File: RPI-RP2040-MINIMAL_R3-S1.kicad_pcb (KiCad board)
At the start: 2 copper layers, 65 x 67 mm, 31 parts, among them J3 Conn_01x04_Pin, J4 Conn_01x04_Socket, P1 USB_C_Plug_USB2.0, U1 NCP1117ST33T3G, U2 W25Q128JVSIQ, U3 RP2040, X1 12MHz

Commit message: flip connector in schematic but not pcb i cant update pcb pls help
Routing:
- added copper zone on F.Cu, net (none)
- removed copper zone on F.Cu, net +1V1
- removed copper zone on F.Cu, net +3V3

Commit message: swap connectors, fix button position
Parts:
- moved J3 13.7 mm to (96.3, 75.1)
- moved J4 13.5 mm to (103.9, 60.3)
- moved ESTOP1 9.90 mm to (54.3, 91.3)
- moved P1 3.50 mm to (100.0, 40.1)
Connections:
- J3 pad 1: Net-(J3-Pin_1) -> GND
- J3 pad 2: unconnected-(J3-Pin_2-Pad2) -> /USB_D+
- J3 pad 3: Net-(J3-Pin_3) -> /USB_D-
- J3 pad 4: Net-(J3-Pin_4) -> VBUS
- J4 pad 1: GND -> /BRIDGE_GND
- J4 pad 2: /USB_D+ -> /BRIDGE_USBD+
- J4 pad 3: /USB_D- -> /BRIDGE_USBD-
- J4 pad 4: VBUS -> /BRIDGE_VBUS
- P1 pad A1: Net-(J3-Pin_1) -> /BRIDGE_GND
- P1 pad A12: Net-(J3-Pin_1) -> /BRIDGE_GND
- P1 pad A4: Net-(J3-Pin_4) -> /BRIDGE_VBUS
- P1 pad A5: Net-(J3-Pin_4) -> /BRIDGE_VBUS
- P1 pad A6: unconnected-(J3-Pin_2-Pad2) -> /BRIDGE_USBD+
- P1 pad A7: Net-(J3-Pin_3) -> /BRIDGE_USBD-
- P1 pad A9: Net-(J3-Pin_4) -> /BRIDGE_VBUS
- P1 pad B1: Net-(J3-Pin_1) -> /BRIDGE_GND
- P1 pad B12: Net-(J3-Pin_1) -> /BRIDGE_GND
- P1 pad B4: Net-(J3-Pin_4) -> /BRIDGE_VBUS
- P1 pad B9: Net-(J3-Pin_4) -> /BRIDGE_VBUS
- P1 pad SH: Net-(J3-Pin_1) -> /BRIDGE_GND
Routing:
- net /BRIDGE_USBD-: track 0.00 -> 22.1 mm
- net /BRIDGE_USBD+: track 0.00 -> 19.8 mm, vias 0 -> 2
- net Net-(J3-Pin_3): track 16.9 -> 0.00 mm
- net unconnected-(J3-Pin_2-Pad2): track 16.9 -> 0.00 mm
- net /USB_D-: track 33.0 -> 19.1 mm
- net VBUS: track 19.8 -> 7.29 mm
- net /BRIDGE_GND: track 0.00 -> 12.1 mm, vias 0 -> 2
- net +3V3: track 28.8 -> 19.2 mm
- net /GPIO0: track 36.2 -> 40.3 mm
- net /USB_D+: track 21.0 -> 19.1 mm
- net Net-(J3-Pin_1): vias 2 -> 0
- added copper zone on F.Cu, net +3V3
- added copper zone on B.Cu, net /BRIDGE_GND
- added copper zone on F.Cu, net /BRIDGE_VBUS
- removed copper zone on B.Cu, net Net-(J3-Pin_1)
- removed copper zone on F.Cu, net Net-(J3-Pin_1)
- removed copper zone on F.Cu, net Net-(J3-Pin_4)
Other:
- board size 65 x 67 mm -> 65 x 70.5 mm
- board text added: "5V"
- board text added: "GND"
- board text removed: "GP7"

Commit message: fix 1V1 connection
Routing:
- net +3V3: track 19.2 -> 48.0 mm
- net +1V1: track 14.2 -> 16.2 mm
- added copper zone on F.Cu, net +1V1
- removed copper zone on F.Cu, net (none)
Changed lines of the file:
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@@
 			(disableapertmacros no)
 			(usegerberextensions no)
-			(usegerberattributes no)
+			(usegerberattributes yes)
 			(usegerberadvancedattributes no)
 			(creategerberjobfile no)
@@
 		(tags "tactile switch SPST angled PTS645VL31-2 LFS C&K Button")
 		(property "Reference" "ESTOP1"
-			(at 2.25 1.68 0)
+			(at 2.3025 -3.82 0)
 			(layer "F.SilkS")
 			(effects
@@
 		)
 		(fp_text user "${REFERENCE}"
-			(at 2.25 1.68 0)
+			(at 2.25 -3.82 0)
 			(layer "F.Fab")
 			(effects
@@
 	)
 	(segment
+		(start 99.63 97.745)
+		(end 99.865 97.51)
+		(width 0.15)
+		(layer "F.Cu")
+		(net "+3V3")
+	)
+	(segment
 		(start 103.1025 101.345)
 		(end 105.465 101.345)
@@
 	)
 	(segment
+		(start 99.735 103)
+		(end 97.5 103)
+		(width 0.2)
+		(layer "F.Cu")
+		(net "+3V3")
+	)
+	(segment
+		(start 96.83 101.345)
+		(end 96.89 101.285)
+		(width 0.15)
+		(layer "F.Cu")
+		(net "+3V3")
+	)
+	(segment
+		(start 102.5 101.345)
+		(end 103.065 101.345)
+		(width 0.15)
+		(layer "F.Cu")
+		(net "+3V3")
+	)
+	(segment
+		(start 99.925 103.12)
+		(end 99.865 103.18)
+		(width 0.15)
+		(layer "F.Cu")
+		(net "+3V3")
+	)
+	(segment
 		(start 99.963474 105.954)
 		(end 101.19 105.954)
@@
 	)
 	(segment
+		(start 102.265 101.11)
+		(end 102.5 101.345)
+		(width 0.15)
+		(layer "F.Cu")
+		(net "+3V3")
+	)
+	(segment
+		(start 101.865 96.945)
+		(end 101.865 100.71)
+		(width 0.15)
+		(layer "F.Cu")
+		(net "+3V3")
+	)
+	(segment
+		(start 97 102.5)
+		(end 97 102)
+		(width 0.2)
+		(layer "F.Cu")
+		(net "+3V3")
+	)
+	(segment
 		(start 100.015001 94.457535)
 		(end 100.015001 95.894999)
@@
 	)
 	(segment
+		(start 101.865 100.71)
+		(end 102.5 101.345)
+		(width 0.15)
+		(layer "F.Cu")
+		(net "+3V3")
+	)
+	(segment
 		(start 93.865 101.345)
 		(end 93.665 101.545)
@@
 	)
 	(segment
+		(start 96.83 97.745)
+		(end 96.265 97.745)
+		(width 0.15)
+		(layer "F.Cu")
+		(net "+3V3")
+	)
+	(segment
 		(start 107.665 86.345)
 		(end 107.665 89.345)
@@
 	)
 	(segment
+		(start 100.265 96.945)
+		(end 99.865 96.945)
+		(width 0.15)
+		(layer "F.Cu")
+		(net "+3V3")
+	)
+	(segment
+		(start 99.865 103.745)
+		(end 99.865 103.13)
+		(width 0.2)
+		(layer "F.Cu")
+		(net "+3V3")
+	)
+	(segment
 		(start 96.2275 101.345)
 		(end 93.865 101.345)
@@
 	)
 	(segment
+		(start 97 101.515)
+		(end 96.83 101.345)
+		(width 0.2)
+		(layer "F.Cu")
+		(net "+3V3")
+	)
+	(segment
+		(start 100.725 103.12)
+		(end 99.925 103.12)
+		(width 0.15)
+		(layer "F.Cu")
+		(net "+3V3")
+	)
+	(segment
+		(start 102.5 101.345)
+		(end 100.725 103.12)
+		(width 0.15)
+		(layer "F.Cu")
+		(net "+3V3")
+	)
+	(segment
 		(start 96.315 85.715)
 		(end 96.315 83.195)
@@
 	)
 	(segment
+		(start 99.865 103.18)
+		(end 99.865 103.745)
+		(width 0.15)
+		(layer "F.Cu")
+		(net "+3V3")
+	)
+	(segment
 		(start 99.665 94.107534)
 		(end 100.015001 94.457535)
@@
 	)
 	(segment
+		(start 97 102)
+		(end 97 101.515)
+		(width 0.2)
+		(layer "F.Cu")
+		(net "+3V3")
+	)
+	(segment
+		(start 100.265 97.11)
+		(end 99.865 97.51)
+		(width 0.15)
+		(layer "F.Cu")
+		(net "+3V3")
+	)
+	(segment
+		(start 99.865 97.51)
+		(end 99.865 96.945)
+		(width 0.15)
+		(layer "F.Cu")
+		(net "+3V3")
+	)
+	(segment
 		(start 100.265 96.9075)
 		(end 100.265 96.144998)
@@
 	)
 	(segment
+		(start 102.265 96.945)
+		(end 102.265 101.11)
+		(width 0.15)
+		(layer "F.Cu")
+		(net "+3V3")
+	)
+	(segment
 		(start 99.865 103.745)
 		(end 99.865 105.855526)
@@
 	)
 	(segment
+		(start 96.265 97.745)
+		(end 99.63 97.745)
+		(width 0.15)
+		(layer "F.Cu")
+		(net "+3V3")
+	)
+	(segment
 		(start 99.865 96.045)
 		(end 99.865 96.9075)
@@
 	)
 	(segment
+		(start 96.89 101.285)
+		(end 96.89 97.805)
+		(width 0.15)
+		(layer "F.Cu")
+		(net "+3V3")
+	)
+	(segment
+		(start 99.865 103.13)
+		(end 99.735 103)
+		(width 0.2)
+		(layer "F.Cu")
+		(net "+3V3")
+	)
+	(segment
 		(start 99.665 93.345)
 		(end 99.665 94.107534)
@@
 	)
 	(segment
+		(start 97.5 103)
+		(end 97 102.5)
+		(width 0.2)
+		(layer "F.Cu")
+		(net "+3V3")
+	)
+	(segment
+		(start 96.89 97.805)
+		(end 96.83 97.745)
+		(width 0.15)
+		(layer "F.Cu")
+		(net "+3V3")
+	)
+	(segment
+		(start 100.265 96.945)
+		(end 100.265 97.11)
+		(width 0.15)
+		(layer "F.Cu")
+		(net "+3V3")
+	)
+	(segment
 		(start 99.865 105.855526)
 		(end 99.963474 105.954)
@@
 	)
 	(segment
+		(start 96.83 101.345)
+		(end 96.265 101.345)
+		(width 0.2)
+		(layer "F.Cu")
+		(net "+3V3")
+	)
+	(segment
 		(start 102.971984 105.954)
 		(end 102.97199 105.954006)
@@
 	)
 	(segment
+		(start 100.755 98.245)
+		(end 100.365 98.245)
+		(width 0.15)
+		(layer "F.Cu")
+		(net "+1V1")
+	)
+	(segment
 		(start 100.265 104.424274)
 		(end 100.265 103.745)
@@
 	)
 	(segment
+		(start 101.465 96.945)
+		(end 101.465 97.535)
+		(width 0.15)
+		(layer "F.Cu")
+		(net "+1V1")
+	)
+	(segment
 		(start 100.99 105.045)
 		(end 101.2 104.835)
@@
 	)
 	(segment
+		(start 101.465 97.535)
+		(end 100.755 98.245)
+		(width 0.15)
+		(layer "F.Cu")
+		(net "+1V1")
+	)
+	(segment
 		(start 98.665 93.345)
 		(end 98.665 93.64)
@@
 	)
 	(zone
+		(net "+1V1")
 		(layer "F.Cu")
 		(hatch edge 0.508)
-		(priority 3)
+		(priority 6)
 		(connect_pads yes
 			(clearance 0.15)
@@
 			)
 		)
-	)
-	(zone
-		(layer "F.Cu")
-		(hatch edge 0.508)
-		(priority 1)
-		(connect_pads yes
-			(clearance 0.15)
-		)
-		(min_thickness 0.15)
-		(fill yes
-			(thermal_gap 0.508)
-			(thermal_bridge_width 0.508)
-			(island_removal_mode 0)
-		)
-		(polygon
-			(pts
-				(xy 102.465 103.145) (xy 96.865 103.145) (xy 96.865 97.545) (xy 99.665 97.545) (xy 100.465 97.545)
-				(xy 102.465 97.545)
-			)
-		)

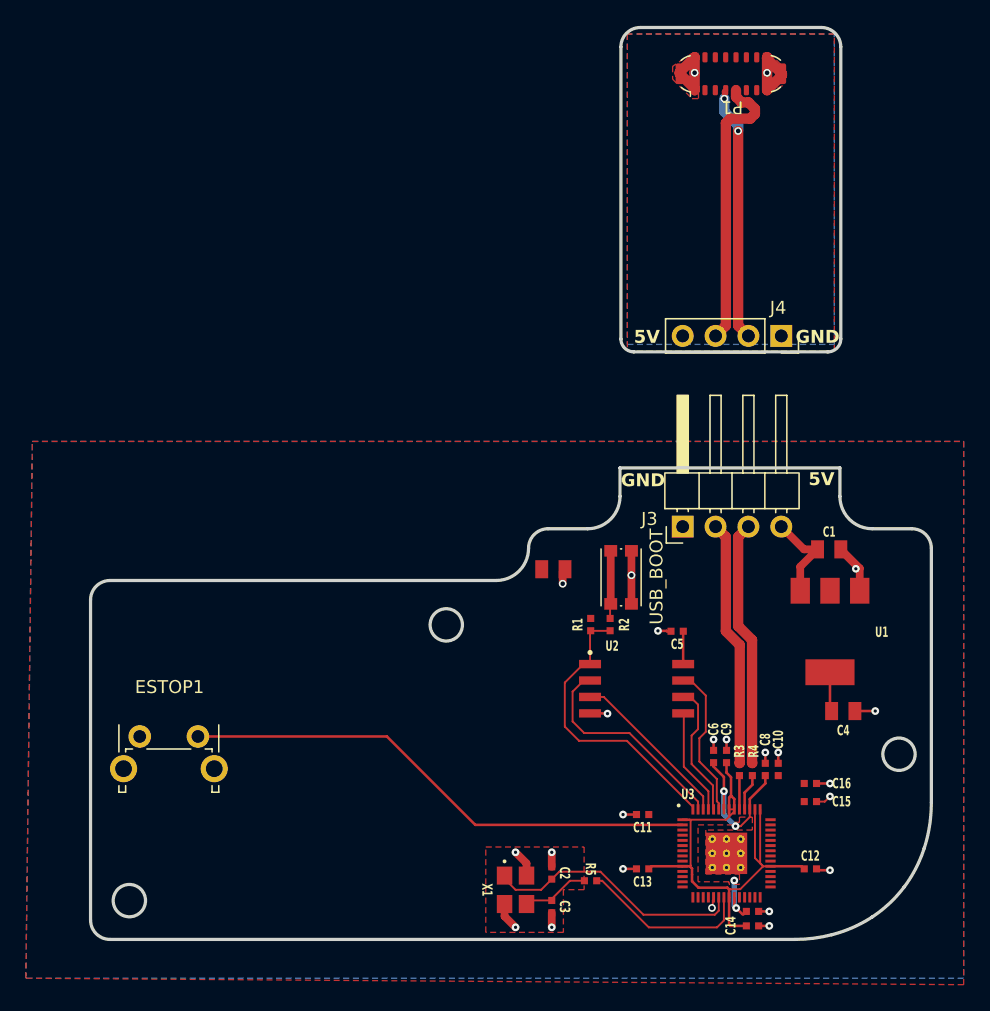
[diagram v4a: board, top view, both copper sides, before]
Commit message: fix offset + teardrops
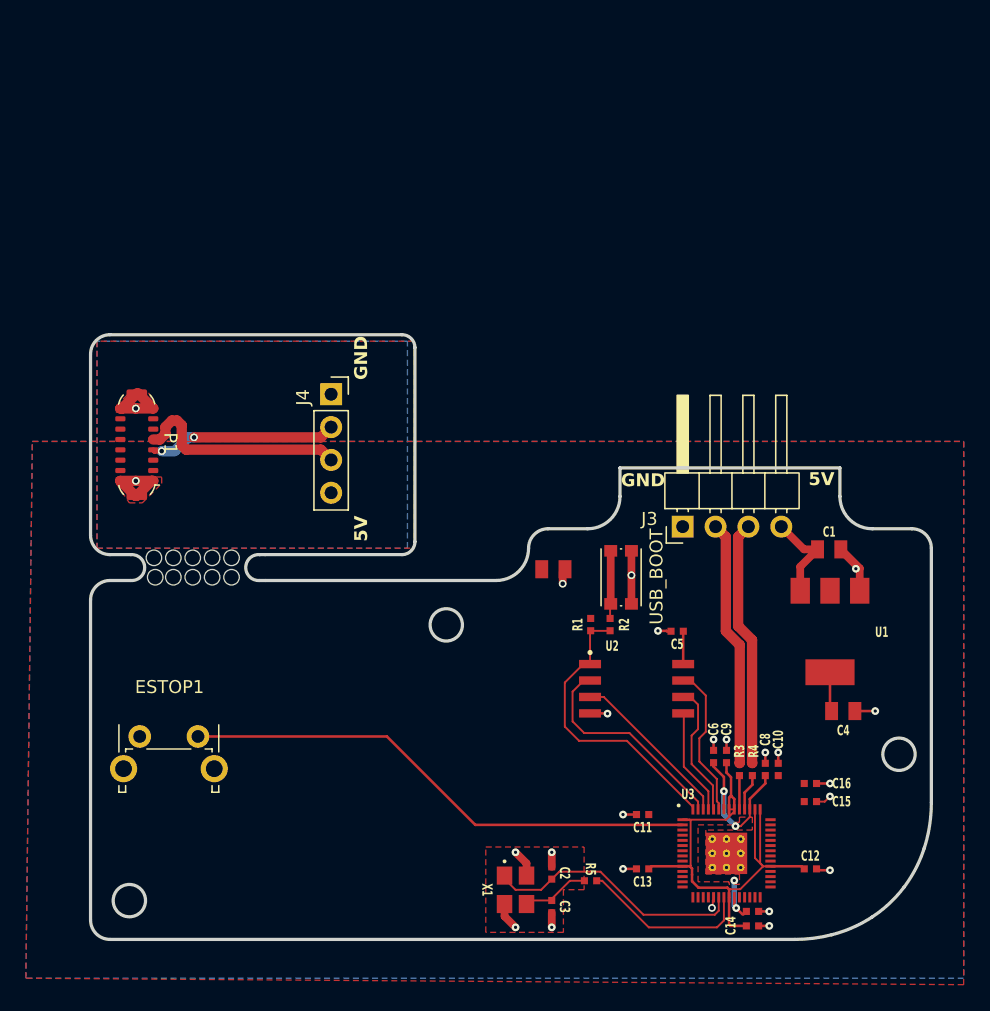
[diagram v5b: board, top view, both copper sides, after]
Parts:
- moved P1 54.1 mm to (54.1, 68.8), turned to 180 degrees
- moved J4 35.1 mm to (69.1, 64.9), turned to 0 degrees
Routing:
- net /BRIDGE_USBD-: track 22.1 -> 16.8 mm
- net /BRIDGE_USBD+: track 19.8 -> 14.6 mm
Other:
- board size 65 x 70.5 mm -> 65 x 46.7 mm

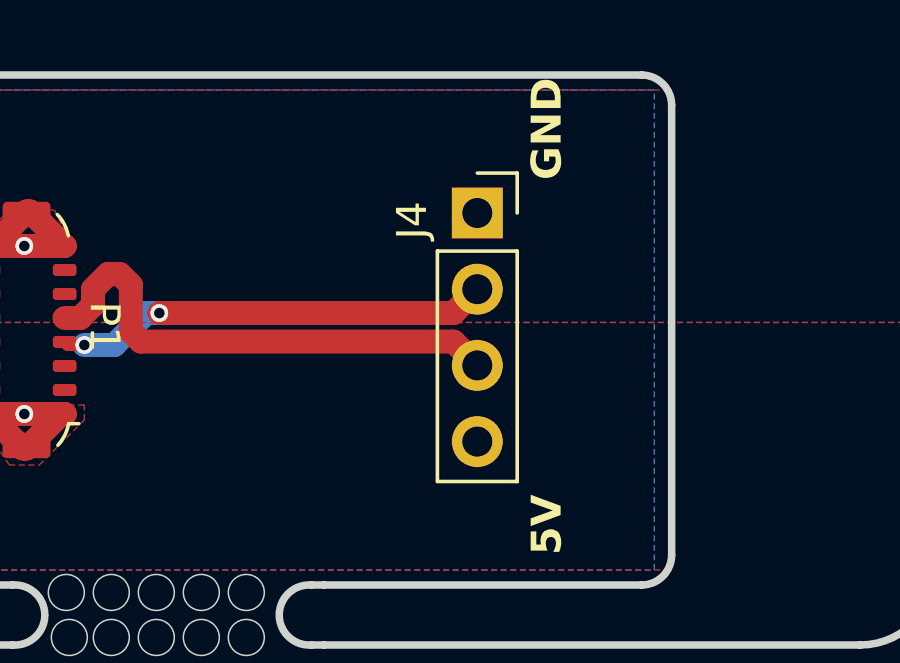
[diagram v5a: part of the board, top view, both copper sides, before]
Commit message: Move header holes on USB bridge board 0.09mm up to center properly on PCB
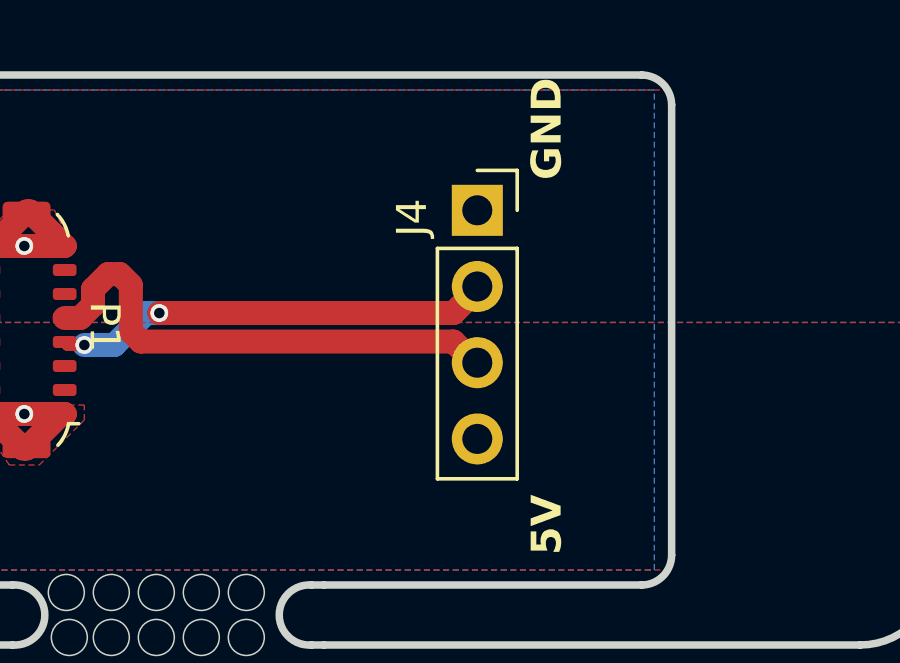
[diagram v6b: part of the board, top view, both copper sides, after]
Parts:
- moved J4 0.09 mm to (69.1, 64.8)
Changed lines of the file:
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@@
 	(footprint "Connector_PinSocket_2.54mm:PinSocket_1x04_P2.54mm_Vertical"
 		(layer "F.Cu")
-		(at 69.099491 64.8517)
+		(at 69.099491 64.7617)
 		(descr "Through hole straight socket strip, 1x04, 2.54mm pitch, single row (from Kicad 4.0.7), script generated")
 		(tags "Through hole socket strip THT 1x04 2.54mm single row")
@@
 	)
 	(segment
-		(start 56.790369 66.888726)
-		(end 56.290369 67.388726)
+		(start 56.290369 67.388726)
+		(end 56.290369 67.92302)
+		(width 0.8)
+		(layer "F.Cu")
+		(net "/BRIDGE_USBD-")
+	)
+	(segment
+		(start 57.185989 66.888726)
+		(end 56.790369 66.888726)
 		(width 0.8)
 		(layer "F.Cu")
@@
 	)
 	(segment
-		(start 69.099491 69.9317)
-		(end 68.304491 69.1367)
+		(start 56.290369 67.92302)
+		(end 55.862379 68.35101)
 		(width 0.8)
 		(layer "F.Cu")
@@
 	)
 	(segment
-		(start 57.185989 66.888726)
-		(end 56.790369 66.888726)
+		(start 57.548963 67.2517)
+		(end 57.185989 66.888726)
 		(width 0.8)
 		(layer "F.Cu")
@@
 	)
 	(segment
-		(start 57.548963 67.2517)
-		(end 57.185989 66.888726)
+		(start 55.862379 68.35101)
+		(end 55.345369 68.35101)
 		(width 0.8)
 		(layer "F.Cu")
@@
 	)
 	(segment
-		(start 56.290369 67.388726)
-		(end 56.290369 67.92302)
+		(start 56.790369 66.888726)
+		(end 56.290369 67.388726)
 		(width 0.8)
 		(layer "F.Cu")
@@
 	)
 	(segment
-		(start 56.290369 67.92302)
-		(end 55.862379 68.35101)
+		(start 69.099491 69.8417)
+		(end 69.009491 69.8417)
 		(width 0.8)
 		(layer "F.Cu")
@@
 	)
 	(segment
-		(start 55.862379 68.35101)
-		(end 55.345369 68.35101)
+		(start 69.009491 69.8417)
+		(end 68.304491 69.1367)
 		(width 0.8)
 		(layer "F.Cu")
@@
 	(group ""
 		(members "0187dbe7-e8c2-450c-8aef-24eb5325b12b" "08ed00fb-4383-4784-9f73-20c77df3a7b1"
-			"11138360-4d5f-4d89-a739-270dc29e5116" "11d1916c-d47f-4933-a1bb-0b739e246e7a"
-			"16541364-1a27-4dd7-b501-a1626643ce21" "1a7b04c7-4b20-4338-920c-d0ed9b441c8f"
-			"1f634cb9-0a72-4fc0-9a18-5bd0b1e5edb4" "257138e0-8c02-4750-9f29-338e21e70f00"
+			"0f70814e-4297-45f3-8a4f-5da671399767" "11138360-4d5f-4d89-a739-270dc29e5116"
+			"1188787d-9b55-4bfb-b533-4372e5e796f7" "16541364-1a27-4dd7-b501-a1626643ce21"
+			"1a7b04c7-4b20-4338-920c-d0ed9b441c8f" "257138e0-8c02-4750-9f29-338e21e70f00"
 			"288ee3e2-d988-40b0-bd9d-ea7de64a6508" "34987f01-9a02-49e2-ae9c-1c0d6e4b879a"
 			"391d9f5c-957c-4d8b-9aeb-af80f551a1b5" "3997b664-7fbc-467e-9989-582e64dc57c5"
 			"3aa0997d-4e33-4535-ab10-8e3ba68186ec" "3d982280-7e01-40f2-92f3-356c6e73459e"
-			"44972b1e-406c-457e-970f-eb112e0e5524" "5f2f9f50-99ce-420f-b235-a8f3d1704220"
 			"61bf2c16-d640-4481-8421-19e295e17405" "6404b271-0a23-4daa-9669-2c53fca30ff3"
 			"664a0fce-0ed9-4c2e-9395-93db82470be6" "6e100cc0-e9b3-4eb8-82b0-da4d9fa4cd20"
 			"7030e1ae-2083-4e0c-b310-6d0bb6cff4db" "71e8feaa-ad86-4fff-ad70-0ec18ffcd9e4"
-			"73ac1332-4a57-49c7-88cf-3913a6cf0b24" "75b64f6e-cabd-4898-9bc3-e9c8d97c8368"
-			"838c6daf-b5d4-4028-91aa-34eeade1a8f6" "86904204-f297-4165-9239-305653056d9d"
+			"7dfde1cc-9cec-43cb-95df-4320f114c371" "838c6daf-b5d4-4028-91aa-34eeade1a8f6"
+			"851576c5-6fba-42c2-b7e2-4225be9d97cc" "86904204-f297-4165-9239-305653056d9d"
 			"8a055d9b-cff1-4a25-8f95-e32bc02e42eb" "8ab97694-2f58-485c-b18e-a6ffee00ea84"
-			"8fe77c87-7bff-4a4e-b616-8c416ee26bfb" "917d41e3-c63f-4df0-84c2-6853d8ba2d19"
+			"8d160bb8-d3f8-4df9-8f31-aee5e533a074" "8fe77c87-7bff-4a4e-b616-8c416ee26bfb"
 			"96195365-365b-4246-ad06-d37062c93fe3" "96b7201e-1eaf-4251-9978-d0425f73d9f5"
-			"9711f30b-6031-4524-9bf1-3bb795aa0915" "a43971be-2932-40ed-909f-1ccc4ce9f7d0"
-			"a83b520f-0de3-44e5-8523-669a51519cc3" "a99811d5-4d79-4925-9e62-cd4e3308589b"
-			"bb80e3a1-be2f-4f57-836c-e9777ddf31bc" "c9b54a73-55b4-4a13-b75f-a99519f7eb76"
-			"d5cff7bb-9d67-4bc1-a76e-e58f62ce7cbf" "d83e0d1f-0c1a-4468-82f2-2602a4141d89"
-			"d8e99e28-de6b-4418-94fc-b0d08fbf36d4" "dfc72a59-37ad-4371-bd75-ba64bde0549d"
-			"ec729c32-55b1-4b8e-a035-bd5ab4f56213" "f4ae312d-250b-4c3b-8e96-93bde8e4b53c"
+			"9711f30b-6031-4524-9bf1-3bb795aa0915" "a3948fb9-4e5c-46f9-8916-b7fb0eadc9ee"
+			"a43971be-2932-40ed-909f-1ccc4ce9f7d0" "a83b520f-0de3-44e5-8523-669a51519cc3"
+			"a99811d5-4d79-4925-9e62-cd4e3308589b" "b8909dc5-20b3-4719-859a-3f4d6f3ab9da"
+			"c221c861-d785-4c85-b519-3ef2c23fa54d" "c66262e8-02d8-4396-8c55-98316d7eaee4"
+			"c9b54a73-55b4-4a13-b75f-a99519f7eb76" "cb457be9-a617-45d4-b949-c92afbf6ee8b"
+			"d5cff7bb-9d67-4bc1-a76e-e58f62ce7cbf" "d8e99e28-de6b-4418-94fc-b0d08fbf36d4"
+			"ec729c32-55b1-4b8e-a035-bd5ab4f56213" "f3b2230d-5e23-4f5b-a36c-16f4308f3633"
+			"f4ae312d-250b-4c3b-8e96-93bde8e4b53c"
 		)
 	)
